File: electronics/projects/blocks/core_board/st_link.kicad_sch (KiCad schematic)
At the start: 4 parts, among them J701 STLINK

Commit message: Update all sheets in core board project. Still looking for processes that give the cleanest update of a design block to a target board design.
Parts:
- renumbered J701 to J601, R701 to R601, R702 to R602, R703 to R603
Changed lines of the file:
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@@
 		(in_pos_files yes)
 		(dnp no)
-		(property "Reference" "R703"
+		(property "Reference" "R603"
 			(at 132.08 88.9 90)
 			(show_name no)
@@
 			)
 			(project "core_board"
-				(path "/efde0c74-5be6-4589-ad87-b4823ac1634b/c87fd2a4-f8d6-4149-89ef-17a7a7e4f014/25dfa83d-e11b-4422-9ae3-56b0a22a4958"
-					(reference "R703")
+				(path "/efde0c74-5be6-4589-ad87-b4823ac1634b/c87fd2a4-f8d6-4149-89ef-17a7a7e4f014/857c3286-f7cf-40ef-a84c-2dc9c0a325d7"
+					(reference "R603")
 					(unit 1)
 				)
@@
 		(in_pos_files yes)
 		(dnp no)
-		(property "Reference" "R702"
+		(property "Reference" "R602"
 			(at 132.08 76.2 90)
 			(show_name no)
@@
 			)
 			(project "core_board"
-				(path "/efde0c74-5be6-4589-ad87-b4823ac1634b/c87fd2a4-f8d6-4149-89ef-17a7a7e4f014/25dfa83d-e11b-4422-9ae3-56b0a22a4958"
-					(reference "R702")
+				(path "/efde0c74-5be6-4589-ad87-b4823ac1634b/c87fd2a4-f8d6-4149-89ef-17a7a7e4f014/857c3286-f7cf-40ef-a84c-2dc9c0a325d7"
+					(reference "R602")
 					(unit 1)
 				)
@@
 		(in_pos_files yes)
 		(dnp no)
-		(property "Reference" "J701"
+		(property "Reference" "J601"
 			(at 149.86 93.98 0)
 			(show_name no)
@@
 			)
 			(project "core_board"
-				(path "/efde0c74-5be6-4589-ad87-b4823ac1634b/c87fd2a4-f8d6-4149-89ef-17a7a7e4f014/25dfa83d-e11b-4422-9ae3-56b0a22a4958"
-					(reference "J701")
+				(path "/efde0c74-5be6-4589-ad87-b4823ac1634b/c87fd2a4-f8d6-4149-89ef-17a7a7e4f014/857c3286-f7cf-40ef-a84c-2dc9c0a325d7"
+					(reference "J601")
 					(unit 1)
 				)
@@
 		(in_pos_files yes)
 		(dnp no)
-		(property "Reference" "R701"
+		(property "Reference" "R601"
 			(at 132.08 68.58 90)
 			(show_name no)
@@
 			)
 			(project "core_board"
-				(path "/efde0c74-5be6-4589-ad87-b4823ac1634b/c87fd2a4-f8d6-4149-89ef-17a7a7e4f014/25dfa83d-e11b-4422-9ae3-56b0a22a4958"
-					(reference "R701")
+				(path "/efde0c74-5be6-4589-ad87-b4823ac1634b/c87fd2a4-f8d6-4149-89ef-17a7a7e4f014/857c3286-f7cf-40ef-a84c-2dc9c0a325d7"
+					(reference "R601")
 					(unit 1)
 				)
@@
 			)
 			(project "core_board"
-				(path "/efde0c74-5be6-4589-ad87-b4823ac1634b/c87fd2a4-f8d6-4149-89ef-17a7a7e4f014/25dfa83d-e11b-4422-9ae3-56b0a22a4958"
+				(path "/efde0c74-5be6-4589-ad87-b4823ac1634b/c87fd2a4-f8d6-4149-89ef-17a7a7e4f014/857c3286-f7cf-40ef-a84c-2dc9c0a325d7"
 					(reference "#PWR0701")
 					(unit 1)

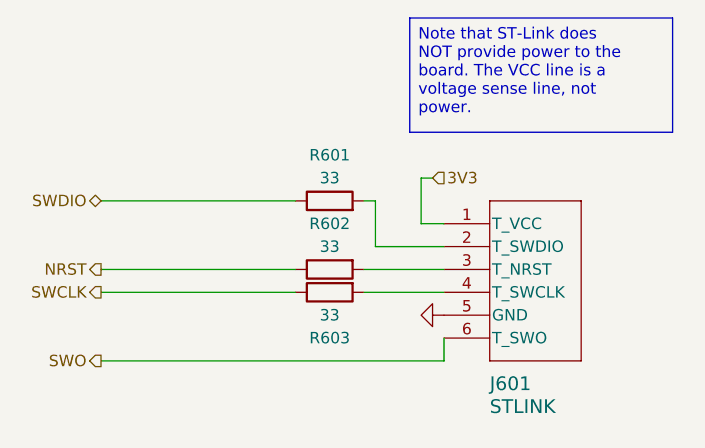
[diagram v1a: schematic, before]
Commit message: Build a version of the core board that passes ERC and DRC checks. Note that this form of the core board puts the system bus header at the extreme edge of the board which will make signal routing from that header nearly impossible if we add a large number of signals. This form only works because the header is sparsely used.
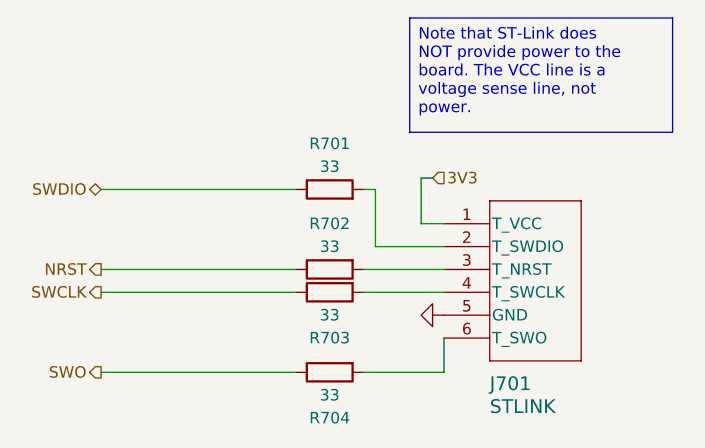
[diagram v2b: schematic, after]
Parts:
- added R704: 33, footprints:Nondescript_R_0402_1005Metric, symbol Device:R
- renumbered J601 to J701, R601 to R701, R602 to R702, R603 to R703
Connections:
- net SWO: now also R704.1; no longer J701.6 (T_SWO)
- new net: J701.6 (T_SWO), R704.2
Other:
- moved on the sheet: R701
